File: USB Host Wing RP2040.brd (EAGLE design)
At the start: 56.3 x 22.9 mm, 60 parts, among them IC1 RP2040_QFN56, J1 USB_A_SMT_FEMALE, Q3 DMG341, SW1 KMR2, SW2 KMR2, U1 2MB Flash, U2 AP2112-3.3, U3 PCA9410AUKZ, X6 USB Type C, Y1 12MHZ

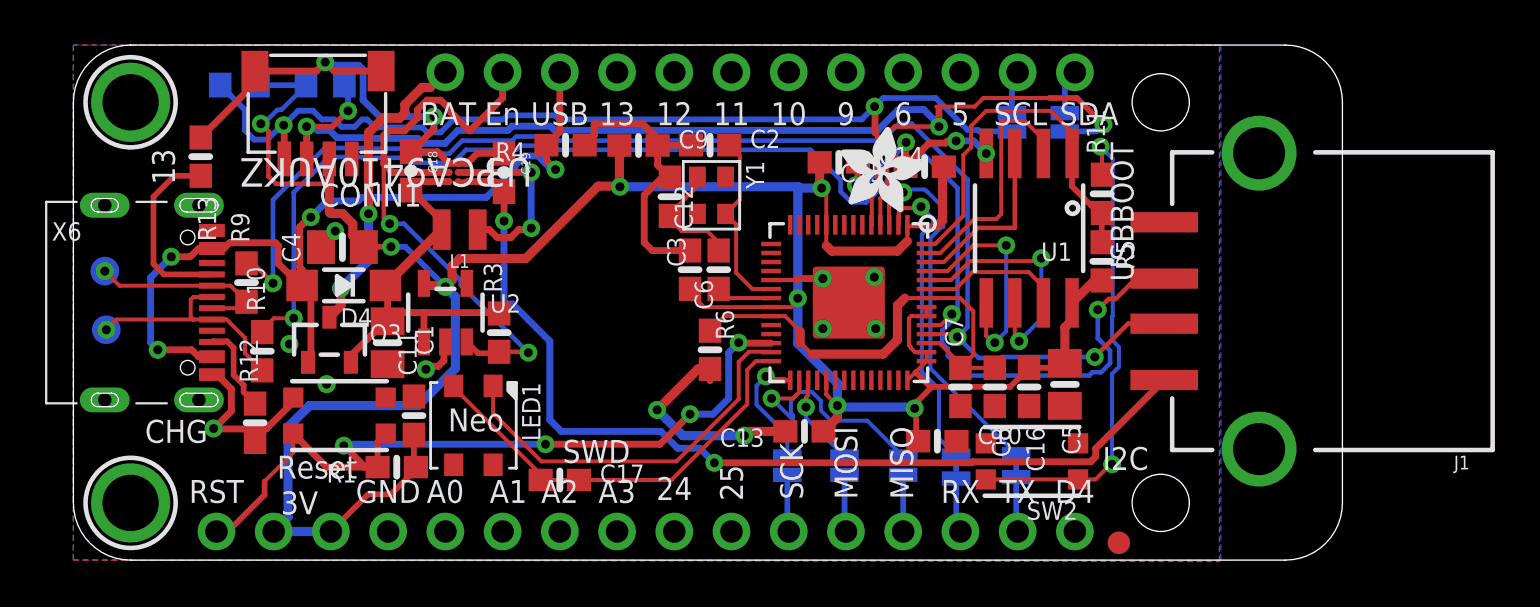
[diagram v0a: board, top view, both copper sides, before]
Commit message: Continued fixes
Modified to replace the boost converter and fix the MOSI/MISO issue.  Also added CS jumpers for SPI users.
Still has air wires & issues.
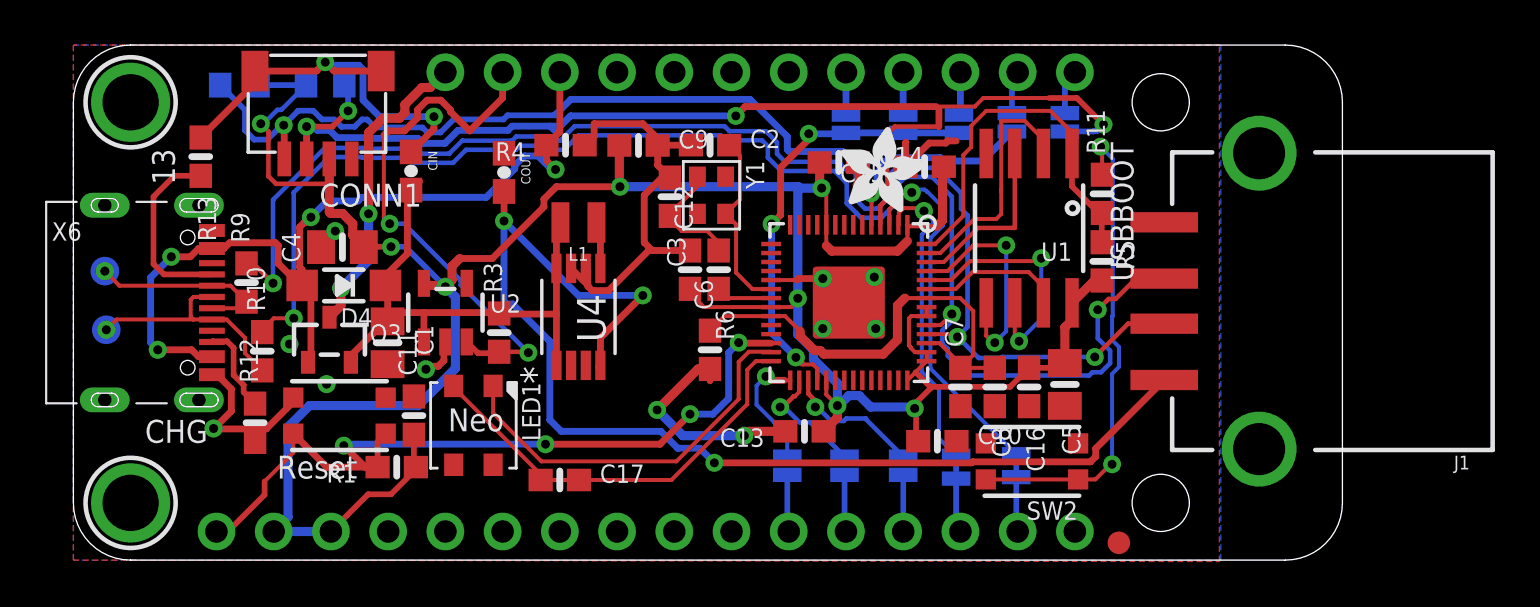
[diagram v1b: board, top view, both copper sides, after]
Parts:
- removed U3: PCA9410AUKZ, PCA9411:WLCSP9_1P24X1P24_NXP
- added JP10, JP11, JP12: JUMPER-SMT_2_NO_SILK, SparkFun-Jumpers:SMT-JUMPER_2_NO_SILK
- added U4: MCP1642B-50I/MS, ATMakers:MSOP8_MCP1642B-50I/MS_MCH
- moved L1 5.28 mm to (22.4, 15.0)
- renumbered C18 to CIN, C19 to COUT
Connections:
- new net N$12: JP12.2, JP3.8
- new net N$13: JP11.2, JP3.9
- new net N$14: JP10.2, JP3.10
- new net SPI_CS: IC1.32, JP10.1, JP11.1, JP12.1
- net EN: no longer U3.B3
- net GND: now also U4.6, U4.7; no longer U3.C1, U3.C2, U3.C3
- net MISO: now also JP5.1; no longer JP6.1
- net MOSI: now also JP6.1; no longer JP5.1
- net N$10: now also U4.5; no longer U3.B1, U3.B2
- net VHI: now also U4.1, U4.8; no longer U3.A3
- net VHOST: now also U4.4; no longer U3.A1, U3.A2
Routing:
- net SPI_CS: track 0.00 -> 19.4 mm, vias 0 -> 3
- net VHOST: track 43.2 -> 52.5 mm, vias 2 -> 3
- net VHI: track 18.3 -> 24.8 mm
- net N$10: track 8.41 -> 2.11 mm, vias 2 -> 0
- net MOSI: track 10.7 -> 5.46 mm
- net GND: track 69.8 -> 66.3 mm, vias 17 -> 13
- net EN: track 27.2 -> 24.2 mm
- net D-: track 57.6 -> 60.1 mm
- net MISO: track 4.14 -> 6.24 mm
- net N$14: track 0.00 -> 1.91 mm
- net N$13: track 0.00 -> 1.88 mm
- net N$12: track 0.00 -> 1.88 mm
- net D+: track 63.8 -> 64.7 mm
- net +3V3: track 121.9 -> 122.6 mm
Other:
- board text removed: "10"
- board text removed: "11"
- board text removed: "12"
- board text removed: "24"
- board text removed: "25"
- board text removed: "5"
- board text removed: "6"
- board text removed: "9"
- board text removed: "A0"
- board text removed: "A1"
- board text removed: "A2"
- board text removed: "A3"
- board text removed: "D4"
- board text removed: "I2C"
- board text removed: "SWD"

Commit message: Update for John
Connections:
- net VBUS: no longer X6.A4B9, X6.B4A9
- net VHOST: now also X6.A4B9, X6.B4A9
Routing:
- net VBUS: track 38.5 -> 28.8 mm, vias 4 -> 2
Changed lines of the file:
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@@
 <layer number="19" name="Unrouted" color="6" fill="1" visible="yes" active="yes"/>
 <layer number="20" name="Dimension" color="15" fill="1" visible="yes" active="yes"/>
-<layer number="21" name="tPlace" color="14" fill="1" visible="no" active="yes"/>
+<layer number="21" name="tPlace" color="14" fill="1" visible="yes" active="yes"/>
 <layer number="22" name="bPlace" color="13" fill="1" visible="yes" active="yes"/>
-<layer number="23" name="tOrigins" color="14" fill="1" visible="no" active="yes"/>
+<layer number="23" name="tOrigins" color="14" fill="1" visible="yes" active="yes"/>
 <layer number="24" name="bOrigins" color="13" fill="1" visible="yes" active="yes"/>
-<layer number="25" name="tNames" color="7" fill="1" visible="no" active="yes"/>
+<layer number="25" name="tNames" color="7" fill="1" visible="yes" active="yes"/>
 <layer number="26" name="bNames" color="7" fill="1" visible="yes" active="yes"/>
 <layer number="27" name="tValues" color="11" fill="1" visible="no" active="yes"/>
@@
 <layer number="37" name="tTest" color="7" fill="1" visible="no" active="yes"/>
 <layer number="38" name="bTest" color="7" fill="1" visible="no" active="yes"/>
-<layer number="39" name="tKeepout" color="4" fill="11" visible="no" active="yes"/>
+<layer number="39" name="tKeepout" color="4" fill="11" visible="yes" active="yes"/>
 <layer number="40" name="bKeepout" color="1" fill="11" visible="yes" active="yes"/>
-<layer number="41" name="tRestrict" color="4" fill="10" visible="no" active="yes"/>
+<layer number="41" name="tRestrict" color="4" fill="10" visible="yes" active="yes"/>
 <layer number="42" name="bRestrict" color="1" fill="10" visible="yes" active="yes"/>
 <layer number="43" name="vRestrict" color="2" fill="10" visible="no" active="yes"/>
@@
 <layer number="49" name="Reference" color="7" fill="1" visible="no" active="yes"/>
 <layer number="50" name="dxf" color="7" fill="1" visible="no" active="no"/>
-<layer number="51" name="tDocu" color="7" fill="1" visible="no" active="yes"/>
+<layer number="51" name="tDocu" color="7" fill="1" visible="yes" active="yes"/>
 <layer number="52" name="bDocu" color="7" fill="1" visible="yes" active="yes"/>
 <layer number="53" name="tGND_GNDA" color="7" fill="9" visible="no" active="no"/>
@@
 <wire x1="10.5435" y1="11.695" x2="10.5435" y2="8.906" width="0.3048" layer="1"/>
 <wire x1="10.5435" y1="8.906" x2="10.4165" y2="8.779" width="0.3048" layer="1"/>
-<contactref element="X6" pad="B4A9"/>
-<contactref element="X6" pad="A4B9"/>
-<via x="4.345" y="13.4634" extent="1-16" drill="0.4"/>
-<wire x1="6.1485" y1="13.83" x2="5.555525" y2="13.83" width="0.3048" layer="1"/>
-<wire x1="5.555525" y1="13.83" x2="5.188925" y2="13.4634" width="0.3048" layer="1"/>
-<wire x1="5.188925" y1="13.4634" x2="4.345" y2="13.4634" width="0.3048" layer="1"/>
-<wire x1="4.345" y1="13.4634" x2="3.429" y2="12.5474" width="0.3048" layer="16"/>
-<wire x1="3.429" y1="9.652" x2="3.7465" y2="9.3345" width="0.3048" layer="16"/>
-<via x="3.7465" y="9.3345" extent="1-16" drill="0.4"/>
-<wire x1="3.7465" y1="9.3345" x2="5.251025" y2="9.3345" width="0.3048" layer="1"/>
-<wire x1="5.555525" y1="9.03" x2="6.1485" y2="9.03" width="0.3048" layer="1"/>
-<wire x1="5.555525" y1="9.03" x2="5.251025" y2="9.3345" width="0.3048" layer="1"/>
-<wire x1="3.429" y1="12.5474" x2="3.429" y2="9.652" width="0.3048" layer="16"/>
 <wire x1="10.0593" y1="12.192" x2="10.1515" y2="12.192" width="0.3048" layer="1"/>
 <contactref element="R4" pad="2"/>
 <wire x1="21.59" y1="21.6535" x2="21.59" y2="19.011" width="0.3048" layer="1"/>
 <wire x1="21.59" y1="19.011" x2="20.994" y2="18.415" width="0.3048" layer="1"/>
-<wire x1="6.1485" y1="13.83" x2="6.677975" y2="13.83" width="0.3048" layer="1"/>
 <wire x1="6.677975" y1="13.83" x2="6.9332375" y2="14.0852625" width="0.3048" layer="1"/>
 <wire x1="8.96945" y1="14.0852625" x2="9.0918" y2="13.9629125" width="0.3048" layer="1"/>
@@
 <wire x1="25.273" y1="11.7475" x2="22.4155" y2="11.7475" width="0.3048" layer="16"/>
 <wire x1="22.4155" y1="11.7475" x2="19.1135" y2="15.0495" width="0.3048" layer="16"/>
+<contactref element="X6" pad="A4B9"/>
+<contactref element="X6" pad="B4A9"/>
+<wire x1="6.1485" y1="13.83" x2="19.1135" y2="15.0495" width="0" layer="19" extent="1-1"/>
+<wire x1="6.1485" y1="9.03" x2="6.1485" y2="13.83" width="0" layer="19" extent="1-1"/>
 </signal>
 <signal name="N$1">

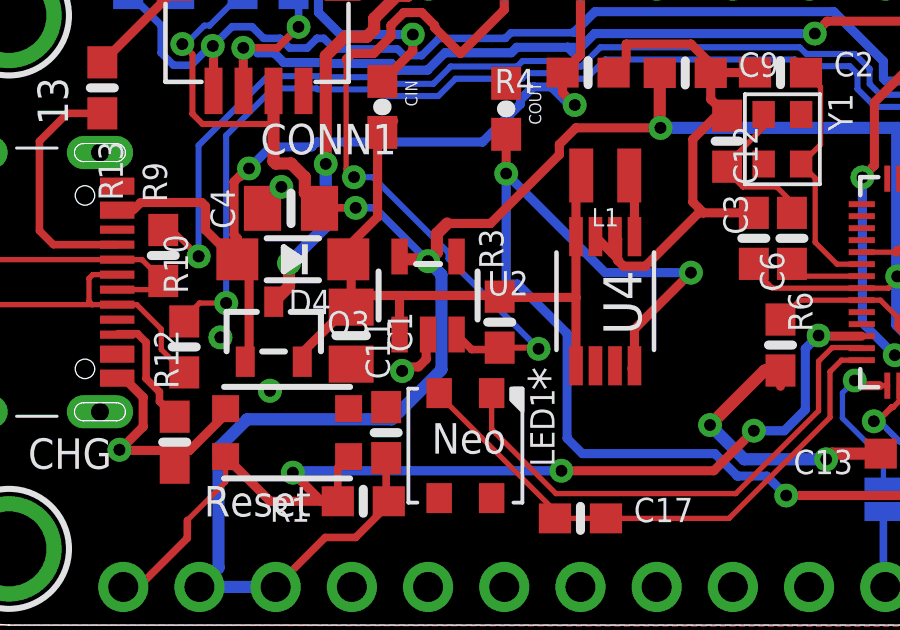
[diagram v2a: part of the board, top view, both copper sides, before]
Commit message: Changed source of linear regulator to VHOST
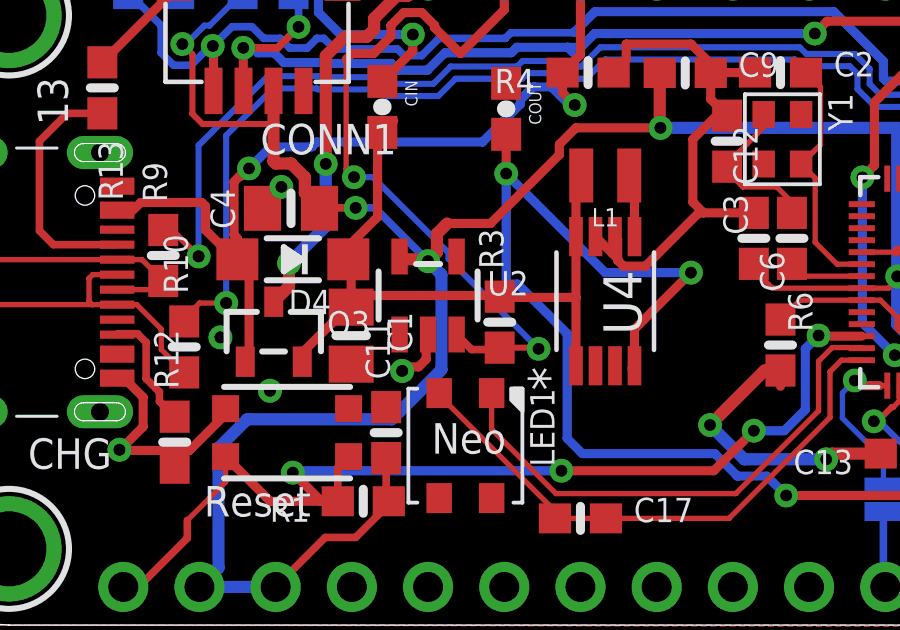
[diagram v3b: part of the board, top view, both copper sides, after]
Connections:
- net VHI: no longer R3.2, U2.1
- net VHOST: now also R3.2, U2.1
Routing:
- net VHI: track 24.8 -> 23.4 mm
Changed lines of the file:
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@@
 <drawing>
 <settings>
-<setting alwaysvectorfont="yes"/>
+<setting alwaysvectorfont="no"/>
 <setting keepoldvectorfont="yes"/>
 <setting verticaltext="up"/>
@@
 <contactref element="Q3" pad="2"/>
 <contactref element="C1" pad="1"/>
-<contactref element="U2" pad="1"/>
-<contactref element="R3" pad="2"/>
-<wire x1="18.8976" y1="10.9465" x2="18.8586" y2="10.9855" width="0.3048" layer="1"/>
 <wire x1="18.8586" y1="10.9855" x2="15.56" y2="10.9855" width="0.3048" layer="1"/>
-<wire x1="15.56" y1="9.6854" x2="15.56" y2="10.9855" width="0.3048" layer="1"/>
 <wire x1="13.9465" y1="10.597" x2="13.8355" y2="10.597" width="0.3048" layer="1"/>
 <wire x1="13.8355" y1="10.597" x2="12.3165" y2="9.078" width="0.3048" layer="1"/>
@@
 <wire x1="21.4405" y1="12.9471" x2="21.4405" y2="14.811" width="0.3048" layer="1"/>
 <wire x1="21.4405" y1="14.811" x2="21.6155" y2="14.986" width="0.3048" layer="1"/>
-<wire x1="18.8976" y1="10.9465" x2="18.9221" y2="10.922" width="0.3048" layer="1"/>
 <wire x1="18.9221" y1="10.922" x2="21.4405" y2="10.922" width="0.3048" layer="1"/>
+<wire x1="18.8586" y1="10.9855" x2="18.9221" y2="10.922" width="0" layer="19" extent="1-1"/>
 </signal>
 <signal name="QSPI_DATA[0]">
@@
 <contactref element="X6" pad="A4B9"/>
 <contactref element="X6" pad="B4A9"/>
-<wire x1="6.1485" y1="13.83" x2="19.1135" y2="15.0495" width="0" layer="19" extent="1-1"/>
-<wire x1="6.1485" y1="9.03" x2="6.1485" y2="13.83" width="0" layer="19" extent="1-1"/>
+<contactref element="U2" pad="1"/>
+<contactref element="R3" pad="2"/>
+<wire x1="15.56" y1="9.6854" x2="18.8976" y2="10.9465" width="0" layer="19" extent="1-1"/>
+<wire x1="19.1135" y1="15.0495" x2="18.8976" y2="10.9465" width="0" layer="19" extent="1-1"/>
+<wire x1="6.1485" y1="9.03" x2="15.56" y2="9.6854" width="0" layer="19" extent="1-1"/>
+<wire x1="6.1485" y1="13.83" x2="6.1485" y2="9.03" width="0" layer="19" extent="1-1"/>
 </signal>
 <signal name="N$1">
